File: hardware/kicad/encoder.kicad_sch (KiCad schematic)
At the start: 5 parts, among them SW31001 RotaryEncoder_Switch_MP

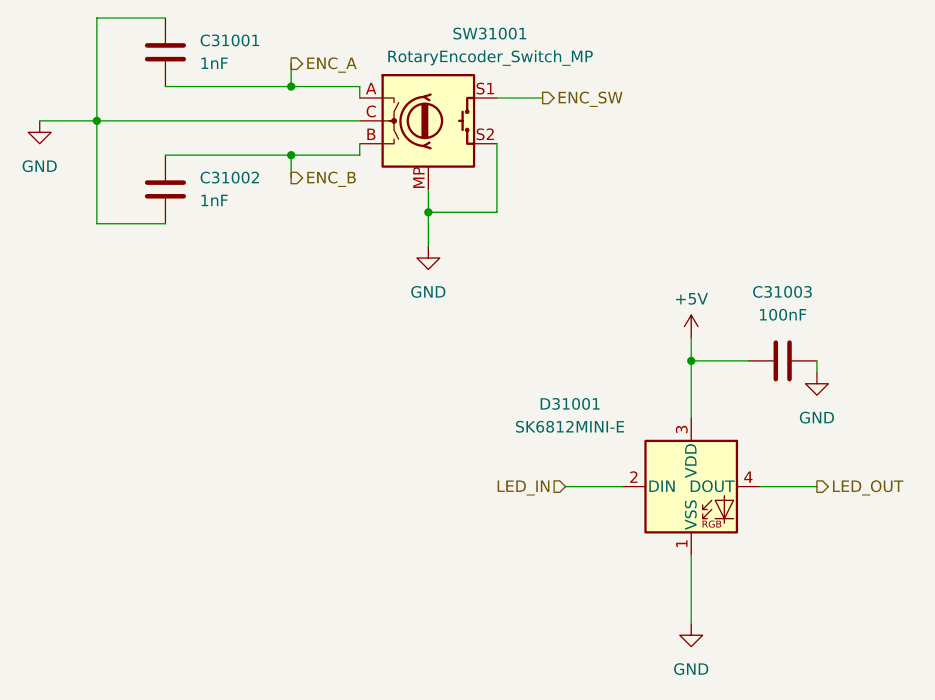
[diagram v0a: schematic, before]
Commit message: "finished" PCB
hardware/kicad/HALE-H8E10.kicad_pcb: Manufacturing: changed the board
  outline. Gergő Törcsvári: updated from the schematic (added C1001,
  C1002, C1004-C1009, H1001-H1012, R1004, R1005 and 5 more; removed
  R1002 and R1003; nets changed on 44 pads); placed C1001, C1002,
  C1004-C1009, H1001-H1012, R1004, R1005 and 4 more; added REF**;
  removed C1004; moved C1003, C2002, C2003, C2006, R1001, TP2001 and
  U1001; routed EN_AUX, EN_LED, +5V_AUX, +5V_LED and 3 more nets;
  rerouted D_CS, DS_BL, DS_RES, E_INT and 21 more nets; and 3 more
  changes.
hardware/kicad/HALE-H8E10.kicad_pro: Gergő Törcsvári excluded 2 DRC
  violations; changed schematic settings.
hardware/kicad/HALE-H8E10.kicad_sch: Gergő Törcsvári added C1001, C1002,
  C1005-C1009, H1001-H1012, R1004, R1005 and 4 more and wired them;
  removed R1002 and R1003; changed 4 parts' fields; changed C1004 wiring
  (pin 1 now on +5V); renamed net unconnected-(U1002-D3-Pad4) to
  /EN_AUX; renamed net unconnected-(U1002-D15-Pad19) to /EN_LED; split
  +5V into +5V_AUX and +5V_LED; and 4 more changes.
hardware/kicad/encoder.kicad_sch: Gergő Törcsvári changed 10 parts'
  fields; renamed net unconnected-(U1002-D3-Pad4) to /EN_AUX; renamed
  net unconnected-(U1002-D15-Pad19) to /EN_LED; split +5V into +5V_AUX
  and +5V_LED.
hardware/kicad/encoders.kicad_sch: Gergő Törcsvári changed 6 parts'
  fields; renamed net unconnected-(U1002-D3-Pad4) to /EN_AUX; renamed
  net unconnected-(U1002-D15-Pad19) to /EN_LED; split +5V into +5V_AUX
  and +5V_LED.
hardware/kicad/key_cell.kicad_sch: Gergő Törcsvári changed 16 parts'
  fields; renamed net unconnected-(U1002-D3-Pad4) to /EN_AUX; renamed
  net unconnected-(U1002-D15-Pad19) to /EN_LED; split +5V into +5V_AUX
  and +5V_LED.
hardware/kicad/keys.kicad_sch: Gergő Törcsvári added R2001 (10K) and
  wired it to /KEYS_CS; changed 6 parts' fields; renamed net
  unconnected-(U1002-D3-Pad4) to /EN_AUX; renamed net
  unconnected-(U1002-D15-Pad19) to /EN_LED; split +5V into +5V_A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
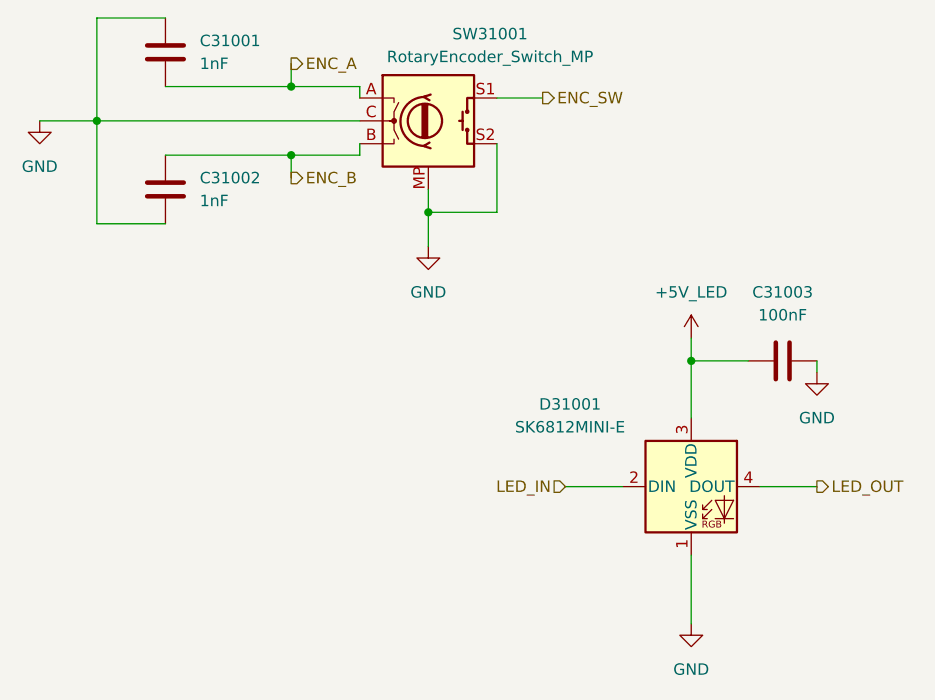
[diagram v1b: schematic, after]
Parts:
- D31001: LCSC (none) -> C5378731
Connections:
- net +5V renamed +5V_LED
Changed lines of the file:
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@@
 			)
 		)
-		(property "LCSC" ""
+		(property "LCSC" "C5378731"
 			(at 115.57 118.11 0)
 			(hide yes)
@@
 		)
 	)
-	(symbol
-		(lib_id "power:+5V")
-		(at 115.57 101.6 0)
-		(unit 1)
-		(body_style 1)
-		(exclude_from_sim no)
-		(in_bom yes)
-		(on_board yes)
-		(in_pos_files yes)
-		(dnp no)
-		(property "Reference" "#PWR031003"
-			(at 115.57 105.41 0)
-			(hide yes)
-			(show_name no)
-			(do_not_autoplace no)
-			(effects
-				(font
-					(size 1.27 1.27)
-				)
-			)
-		)
-		(property "Value" "+5V"
-			(at 115.57 97.282 0)
-			(show_name no)
-			(do_not_autoplace no)
-			(effects
-				(font
-					(size 1.27 1.27)
-				)
-			)
-		)
-		(property "Footprint" ""
-			(at 115.57 101.6 0)
-			(hide yes)
-			(show_name no)
-			(do_not_autoplace no)
-			(effects
-				(font
-					(size 1.27 1.27)
-				)
-			)
-		)
-		(property "Datasheet" ""
-			(at 115.57 101.6 0)
-			(hide yes)
-			(show_name no)
-			(do_not_autoplace no)
-			(effects
-				(font
-					(size 1.27 1.27)
-				)
-			)
-		)
-		(property "Description" "Power symbol creates a global label with name \"+5V\""
-			(at 115.57 101.6 0)
-			(hide yes)
-			(show_name no)
-			(do_not_autoplace no)
-			(effects
-				(font
-					(size 1.27 1.27)
-				)
-			)
-		)
-		(pin "1"
-		)
-		(instances
-			(project "HALE-H8E10"
-				(path "/95d89127-9479-4179-8532-6fc4e4c352d8/b92ca440-41fc-4f69-ab39-b4c036ee6d57/190c6ed3-1a42-4715-a32a-8245a11d6fd1"
-					(reference "#PWR033003")
-					(unit 1)
-				)
-				(path "/95d89127-9479-4179-8532-6fc4e4c352d8/b92ca440-41fc-4f69-ab39-b4c036ee6d57/22f422a4-276f-47e2-a2d4-53108e4c201e"
-					(reference "#PWR037003")
-					(unit 1)
-				)
-				(path "/95d89127-9479-4179-8532-6fc4e4c352d8/b92ca440-41fc-4f69-ab39-b4c036ee6d57/2eb38094-c0b7-44ab-8831-a6192a8b5132"
-					(reference "#PWR039003")
-					(unit 1)
-				)
-				(path "/95d89127-9479-4179-8532-6fc4e4c352d8/b92ca440-41fc-4f69-ab39-b4c036ee6d57/3252edd8-2663-4144-b5ee-180a3f4925ce"
-					(reference "#PWR040003")
-					(unit 1)
-				)
-				(path "/95d89127-9479-4179-8532-6fc4e4c352d8/b92ca440-41fc-4f69-ab39-b4c036ee6d57/8694b622-cffc-443d-a943-b6c742454971"
-					(reference "#PWR031003")
-					(unit 1)
-				)
-				(path "/95d89127-9479-4179-8532-6fc4e4c352d8/b92ca440-41fc-4f69-ab39-b4c036ee6d57/8f1bd5c9-3013-4628-860e-e677149ba41e"
-					(reference "#PWR036003")
-					(unit 1)
-				)
-				(path "/95d89127-9479-4179-8532-6fc4e4c352d8/b92ca440-41fc-4f69-ab39-b4c036ee6d57/b9112ac5-0e11-40d8-9e01-6e2240b65ee2"
-					(reference "#PWR038003")
-					(unit 1)
-				)
-				(path "/95d89127-9479-4179-8532-6fc4e4c352d8/b92ca440-41fc-4f69-ab39-b4c036ee6d57/bc963598-3dd1-4e5d-a6bc-ecbbb83733e7"
-					(reference "#PWR035003")
-					(unit 1)
-				)
-				(path "/95d89127-9479-4179-8532-6fc4e4c352d8/b92ca440-41fc-4f69-ab39-b4c036ee6d57/e910f79a-11f3-4611-8566-8e965d7b9a8e"
-					(reference "#PWR034003")
-					(unit 1)
-				)
-				(path "/95d89127-9479-4179-8532-6fc4e4c352d8/b92ca440-41fc-4f69-ab39-b4c036ee6d57/f8b05a19-a7ce-4f92-9338-66786138864b"
-					(reference "#PWR032003")
-					(unit 1)
-				)
-			)
-		)
-	)
 	(wire
 		(pts
@@
 		(color 0 0 0 0)
 	)
+	(symbol
+		(lib_id "power:+5VL")
+		(at 115.57 101.6 0)
+		(unit 1)
+		(body_style 1)
+		(exclude_from_sim no)
+		(in_bom yes)
+		(on_board yes)
+		(in_pos_files yes)
+		(dnp no)
+		(fields_autoplaced yes)
+		(property "Reference" "#PWR031003"
+			(at 115.57 105.41 0)
+			(hide yes)
+			(show_name no)
+			(do_not_autoplace no)
+			(effects
+				(font
+					(size 1.27 1.27)
+				)
+			)
+		)
+		(property "Value" "+5V_LED"
+			(at 115.57 96.52 0)
+			(show_name no)
+			(do_not_autoplace no)
+			(effects
+				(font
+					(size 1.27 1.27)
+				)
+			)
+		)
+		(property "Footprint" ""
+			(at 115.57 101.6 0)
+			(hide yes)
+			(show_name no)
+			(do_not_autoplace no)
+			(effects
+				(font
+					(size 1.27 1.27)
+				)
+			)
+		)
+		(property "Datasheet" ""
+			(at 115.57 101.6 0)
+			(hide yes)
+			(show_name no)
+			(do_not_autoplace no)
+			(effects
+				(font
+					(size 1.27 1.27)
+				)
+			)
+		)
+		(property "Description" "Power symbol creates a global label with name \"+5VL\""
+			(at 115.57 101.6 0)
+			(hide yes)
+			(show_name no)
+			(do_not_autoplace no)
+			(effects
+				(font
+					(size 1.27 1.27)
+				)
+			)
+		)
+		(pin "1"
+		)
+		(instances
+			(project "HALE-H8E10"
+				(path "/95d89127-9479-4179-8532-6fc4e4c352d8/b92ca440-41fc-4f69-ab39-b4c036ee6d57/190c6ed3-1a42-4715-a32a-8245a11d6fd1"
+					(reference "#PWR033003")
+					(unit 1)
+				)
+				(path "/95d89127-9479-4179-8532-6fc4e4c352d8/b92ca440-41fc-4f69-ab39-b4c036ee6d57/22f422a4-276f-47e2-a2d4-53108e4c201e"
+					(reference "#PWR037003")
+					(unit 1)
+				)
+				(path "/95d89127-9479-4179-8532-6fc4e4c352d8/b92ca440-41fc-4f69-ab39-b4c036ee6d57/2eb38094-c0b7-44ab-8831-a6192a8b5132"
+					(reference "#PWR039003")
+					(unit 1)
+				)
+				(path "/95d89127-9479-4179-8532-6fc4e4c352d8/b92ca440-41fc-4f69-ab39-b4c036ee6d57/3252edd8-2663-4144-b5ee-180a3f4925ce"
+					(reference "#PWR040003")
+					(unit 1)
+				)
+				(path "/95d89127-9479-4179-8532-6fc4e4c352d8/b92ca440-41fc-4f69-ab39-b4c036ee6d57/8694b622-cffc-443d-a943-b6c742454971"
+					(reference "#PWR031003")
+					(unit 1)
+				)
+				(path "/95d89127-9479-4179-8532-6fc4e4c352d8/b92ca440-41fc-4f69-ab39-b4c036ee6d57/8f1bd5c9-3013-4628-860e-e677149ba41e"
+					(reference "#PWR036003")
+					(unit 1)
+				)
+				(path "/95d89127-9479-4179-8532-6fc4e4c352d8/b92ca440-41fc-4f69-ab39-b4c036ee6d57/b9112ac5-0e11-40d8-9e01-6e2240b65ee2"
+					(reference "#PWR038003")
+					(unit 1)
+				)
+				(path "/95d89127-9479-4179-8532-6fc4e4c352d8/b92ca440-41fc-4f69-ab39-b4c036ee6d57/bc963598-3dd1-4e5d-a6bc-ecbbb83733e7"
+					(reference "#PWR035003")
+					(unit 1)
+				)
+				(path "/95d89127-9479-4179-8532-6fc4e4c352d8/b92ca440-41fc-4f69-ab39-b4c036ee6d57/e910f79a-11f3-4611-8566-8e965d7b9a8e"
+					(reference "#PWR034003")
+					(unit 1)
+				)
+				(path "/95d89127-9479-4179-8532-6fc4e4c352d8/b92ca440-41fc-4f69-ab39-b4c036ee6d57/f8b05a19-a7ce-4f92-9338-66786138864b"
+					(reference "#PWR032003")
+					(unit 1)
+				)
+			)
+		)
+	)
 )

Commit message: rev, and minor adjustements
hardware/kicad/HALE-H8E10.kicad_pcb: Gergő Törcsvári moved K21001,
  K22001, K23001, K24001, K25001, K26001, K27001 and K28001; title
  block: date - → ${RELEASE_DATE}, rev - → ${REV}, title - → HALE-H8E10;
  tidied the silkscreen.
hardware/kicad/HALE-H8E10.kicad_pro: Manufacturing: changed the IPC-2581
  settings. Gergő Törcsvári: RELEASE_DATE - → 2026-10-20; REV - → 1.0;
  changed schematic settings.
hardware/kicad/HALE-H8E10.kicad_sch: Gergő Törcsvári title block: date
  2026-10-12 → ${RELEASE_DATE}, rev A → ${REV}.
hardware/kicad/encoder.kicad_sch: Gergő Törcsvári changed 10 parts'
  fields.
hardware/kicad/key_cell.kicad_sch: Gergő Törcsvári changed 8 parts'
  fields.
hardware/kicad/pcbjam.lock.json: Library lockfile regenerated.

Checks: ERC: 2 errors in HALE-H8E10.kicad_sch (pin to pin ×2) · DRC clean

PCBJam-Commit: 7f3340a3-7d55-4157-ad73-e17d7d28c5bf
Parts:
- D31001: LCSC C5378731 -> C5149201
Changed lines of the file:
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@@
 			)
 		)
-		(property "LCSC" "C5378731"
+		(property "LCSC" "C5149201"
 			(at 115.57 118.11 0)
 			(hide yes)
